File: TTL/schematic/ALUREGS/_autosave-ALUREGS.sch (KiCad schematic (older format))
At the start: 20 parts

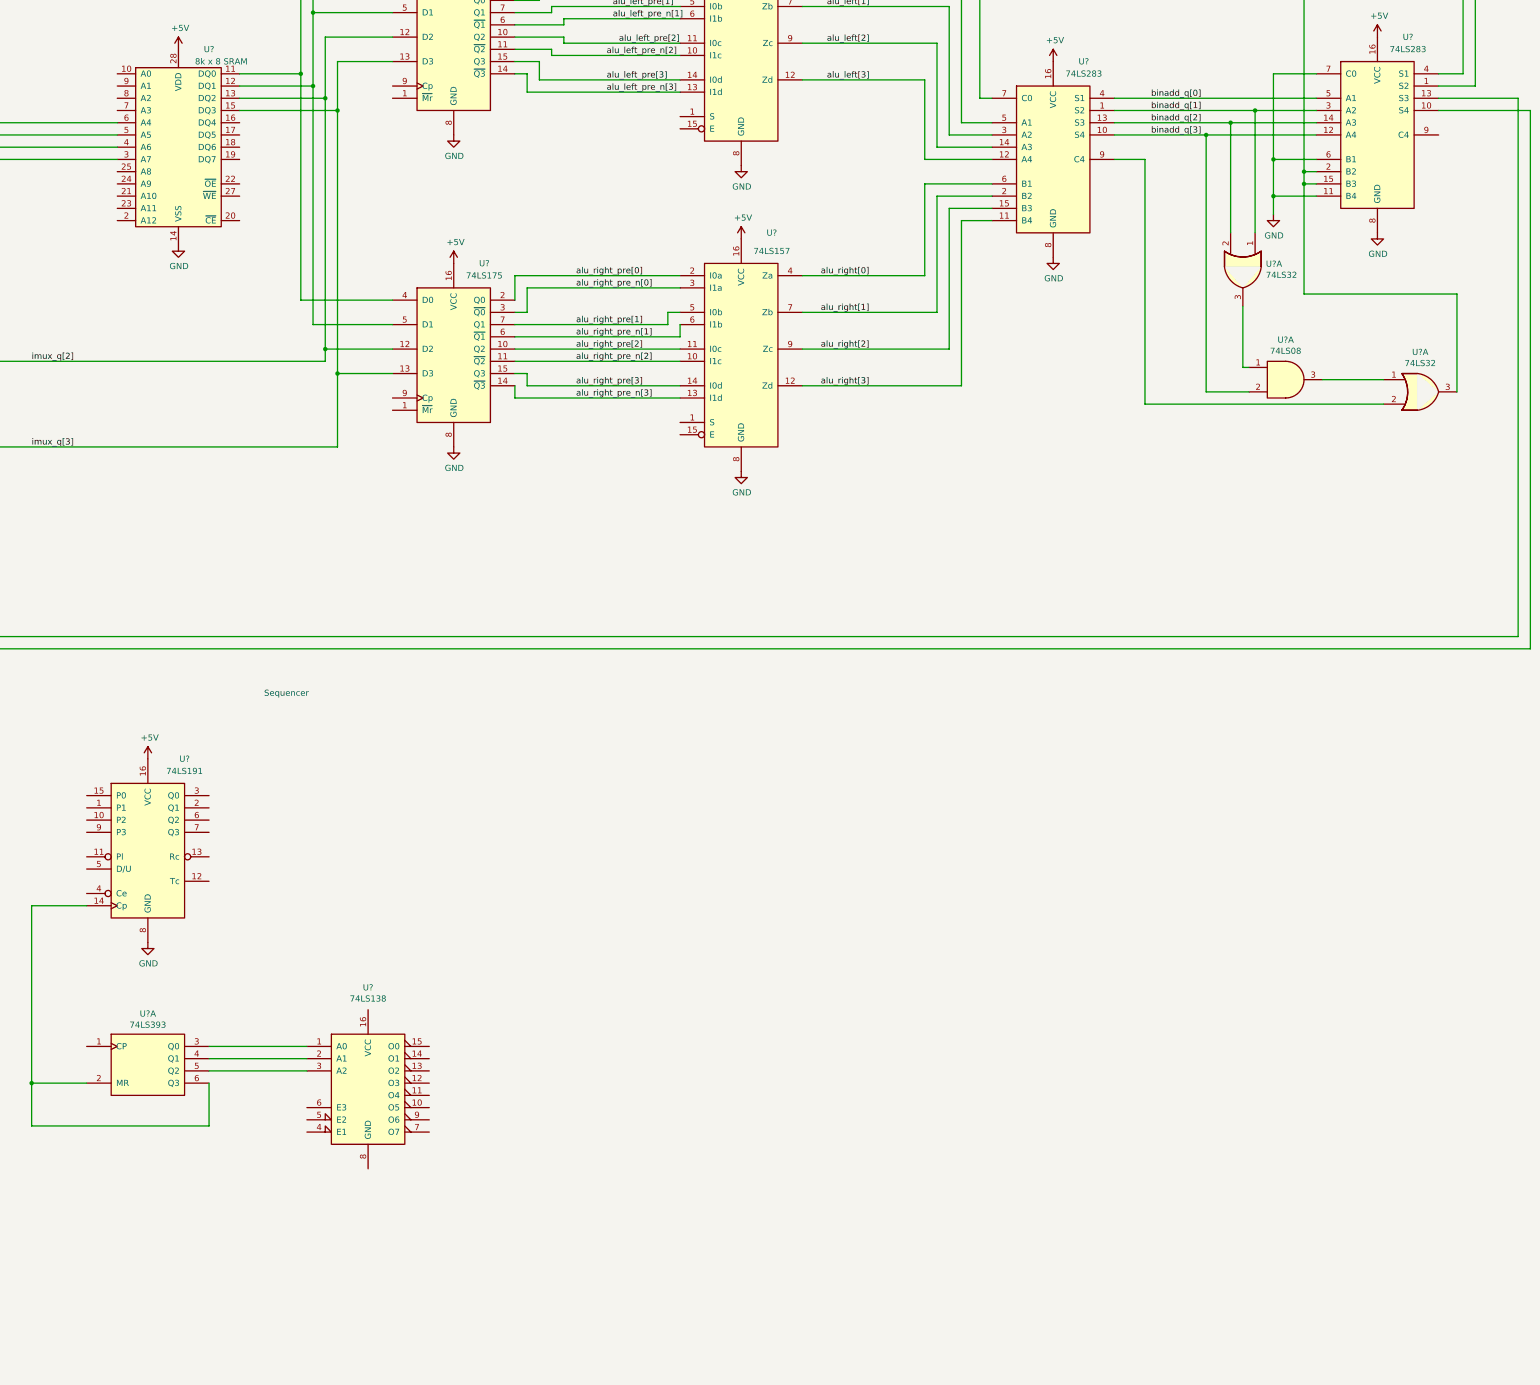
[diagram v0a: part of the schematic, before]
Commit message: Added docu, work in progress schematics and vhdl
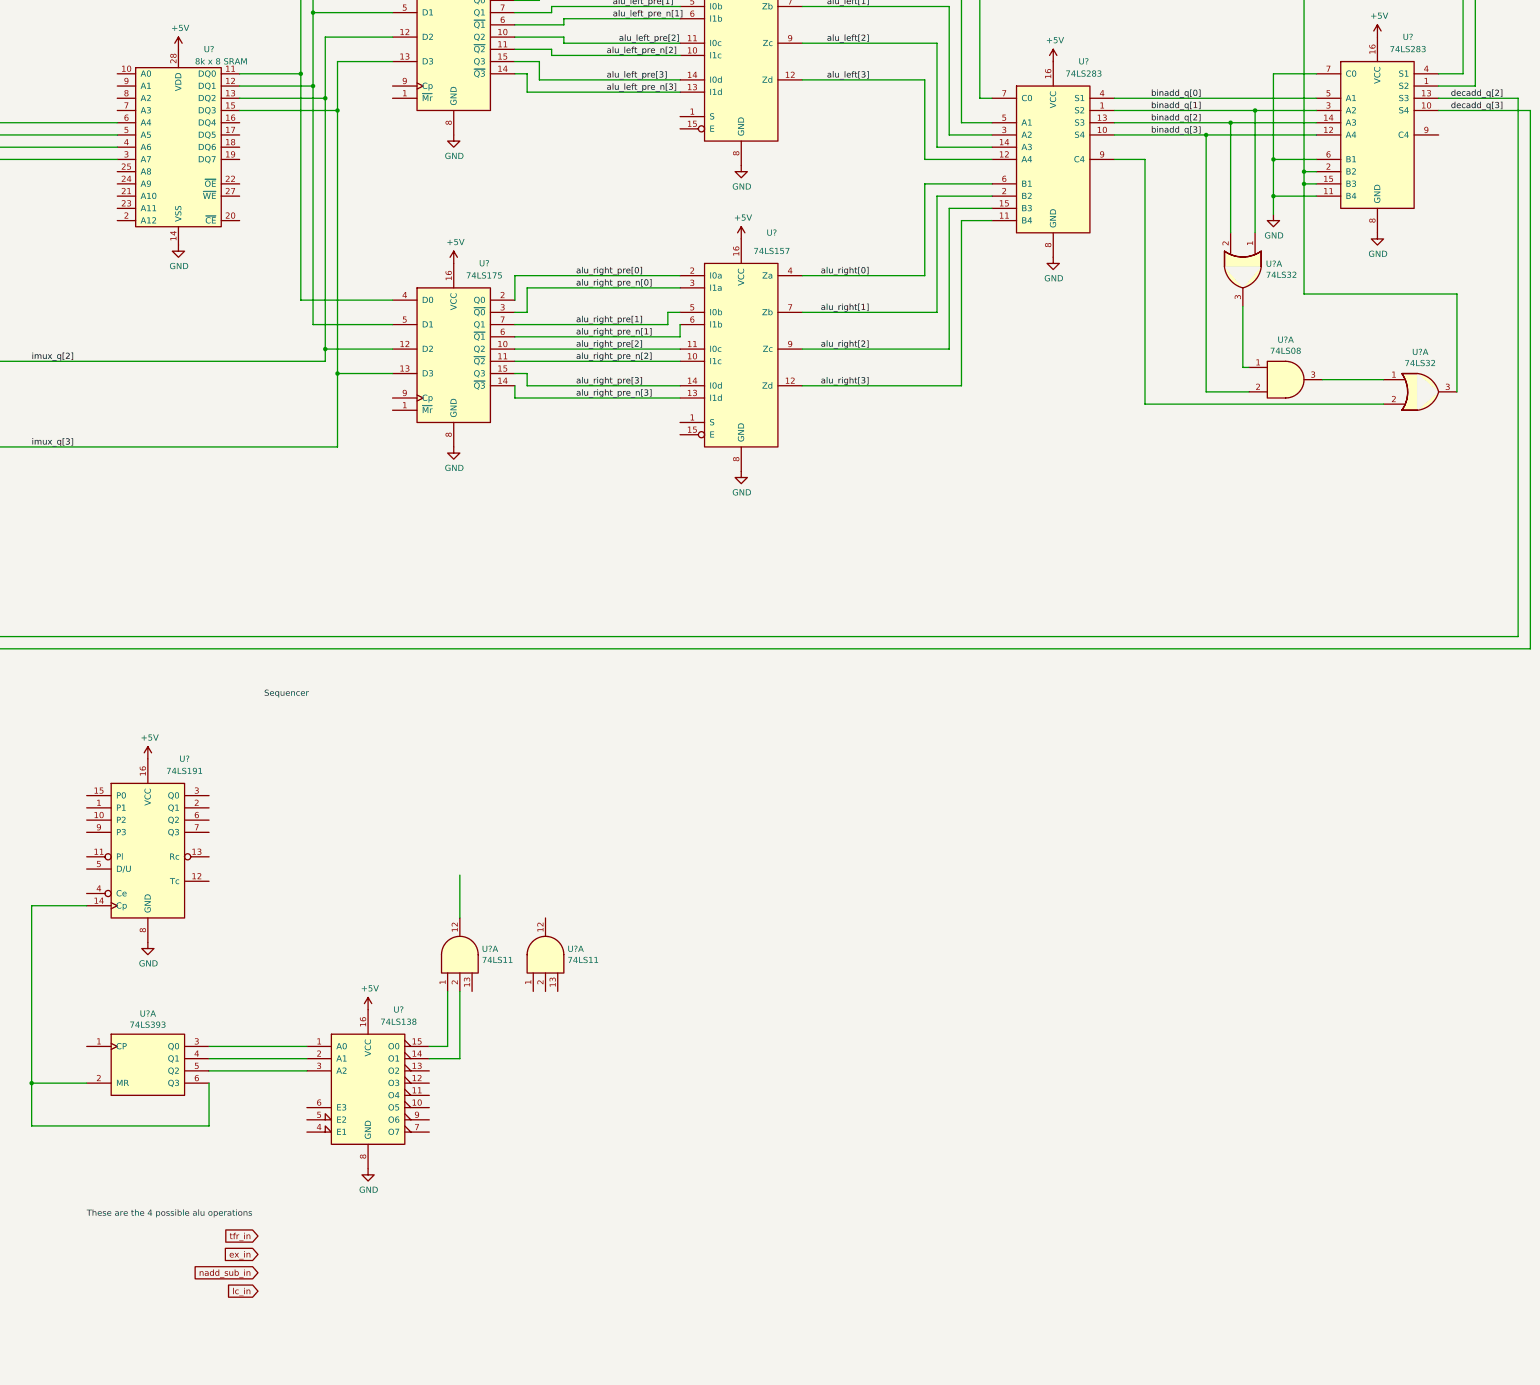
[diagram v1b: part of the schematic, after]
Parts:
- added U? (x2): 74LS11, symbol 74xx:74LS11
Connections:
- net +5V: now also U?.16 (VCC)
- net GND: now also U?.8 (GND)
- net decadd_q[3]: now reaches U?.10 (I0b), U?.10 (S4)
- net decadd_q[2]: now reaches U?.13 (S3), U?.6 (I0a)
- net at U?.14 (O1): now also U?.2
- net at U?.15 (O0): now also U?.1
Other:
- note added: "These are the 4 possible alu operations"
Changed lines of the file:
@@
 U 1 1 60C78169
 P 12900 12600
-F 0 "U?" H 12900 13381 50  0000 C CNN
-F 1 "74LS138" H 12900 13290 50  0000 C CNN
+F 0 "U?" H 13150 13200 50  0000 C CNN
+F 1 "74LS138" H 13150 13100 50  0000 C CNN
 F 2 "" H 12900 12600 50  0001 C CNN
 F 3 "http://www.ti.com/lit/gpn/sn74LS138" H 12900 12600 50  0001 C CNN
@@
 Wire Wire Line
 	14500 3900 15450 3900
+$Comp
+L 74xx:74LS11 U?
+U 1 1 60B30210
+P 13650 11550
+F 0 "U?" V 13696 11370 50  0000 R CNN
+F 1 "74LS11" V 13605 11370 50  0000 R CNN
+F 2 "" H 13650 11550 50  0001 C CNN
+F 3 "http://www.ti.com/lit/gpn/sn74LS11" H 13650 11550 50  0001 C CNN
+	1    13650 11550
+	0    -1   -1   0
+$EndComp
+$Comp
+L 74xx:74LS11 U?
+U 1 1 60B34308
+P 14350 11550
+F 0 "U?" V 14396 11370 50  0000 R CNN
+F 1 "74LS11" V 14305 11370 50  0000 R CNN
+F 2 "" H 14350 11550 50  0001 C CNN
+F 3 "http://www.ti.com/lit/gpn/sn74LS11" H 14350 11550 50  0001 C CNN
+	1    14350 11550
+	0    -1   -1   0
+$EndComp
+Wire Wire Line
+	13400 12300 13550 12300
+Wire Wire Line
+	13550 12300 13550 11850
+Wire Wire Line
+	13400 12400 13650 12400
+Wire Wire Line
+	13650 12400 13650 11850
+Wire Wire Line
+	13650 11250 13650 10900
+Text GLabel 12000 13850 0    50   Input ~ 0
+tfr_in
+Text GLabel 12000 14000 0    50   Input ~ 0
+ex_in
+Text GLabel 12000 14150 0    50   Input ~ 0
+nadd_sub_in
+Text GLabel 12000 14300 0    50   Input ~ 0
+lc_in
+Text Notes 10600 13700 0    50   ~ 0
+These are the 4 possible alu operations
+$Comp
+L power:GND #PWR?
+U 1 1 60B60925
+P 12900 13300
+F 0 "#PWR?" H 12900 13050 50  0001 C CNN
+F 1 "GND" H 12905 13127 50  0000 C CNN
+F 2 "" H 12900 13300 50  0001 C CNN
+F 3 "" H 12900 13300 50  0001 C CNN
+	1    12900 13300
+	1    0    0    -1
+$EndComp
+$Comp
+L power:+5V #PWR?
+U 1 1 60B60FF9
+P 12900 12000
+F 0 "#PWR?" H 12900 11850 50  0001 C CNN
+F 1 "+5V" H 12915 12173 50  0000 C CNN
+F 2 "" H 12900 12000 50  0001 C CNN
+F 3 "" H 12900 12000 50  0001 C CNN
+	1    12900 12000
+	1    0    0    -1
+$EndComp
+Text Label 21750 4550 0    50   ~ 0
+decadd_q[2]
+Text Label 21750 4650 0    50   ~ 0
+decadd_q[3]
 $EndSCHEMATC
